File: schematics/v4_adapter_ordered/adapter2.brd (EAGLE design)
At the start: 83.1 x 45.2 mm, 40 parts, among them X1 USB-A-HU, X10 USB-A-HU, X11 USB-A-HU, X12 USB-A-HU, X13 USB-A-HU, X14 USB-A-HU, X15 USB-A-HU, X16 USB-A-HU, X17 USB-A-HU, X18 USB-A-HU, X19 USB-A-HU, X2 USB-A-HU, X20 USB-A-HU, X21 USB-A-HU, X22 USB-A-HU, X23 USB-A-HU, X24 USB-A-HU, X25 USB-A-HU, X26 USB-A-HU, X27 USB-A-HU, X28 USB-A-HU, X29 USB-A-HU, X3 USB-A-HU, X30 USB-A-HU, X31 USB-A-HU, X32 USB-A-HU, X4 USB-A-HU, X49 USB-A-HU, X5 USB-A-HU, X50 USB-A-HU, X51 USB-A-HU, X52 USB-A-HU, X53 USB-A-HU, X54 USB-A-HU, X55 USB-A-HU, X56 USB-A-HU, X6 USB-A-HU, X7 USB-A-HU, X8 USB-A-HU, X9 USB-A-HU

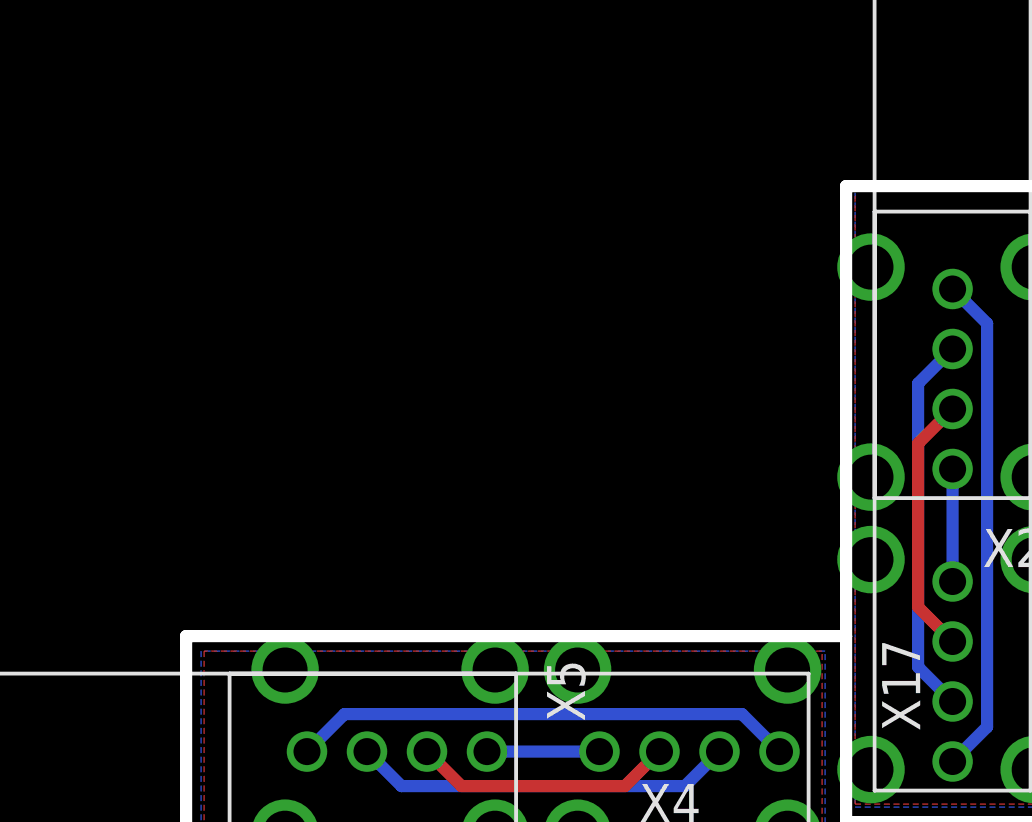
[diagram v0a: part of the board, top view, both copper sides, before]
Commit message: sch + adapter
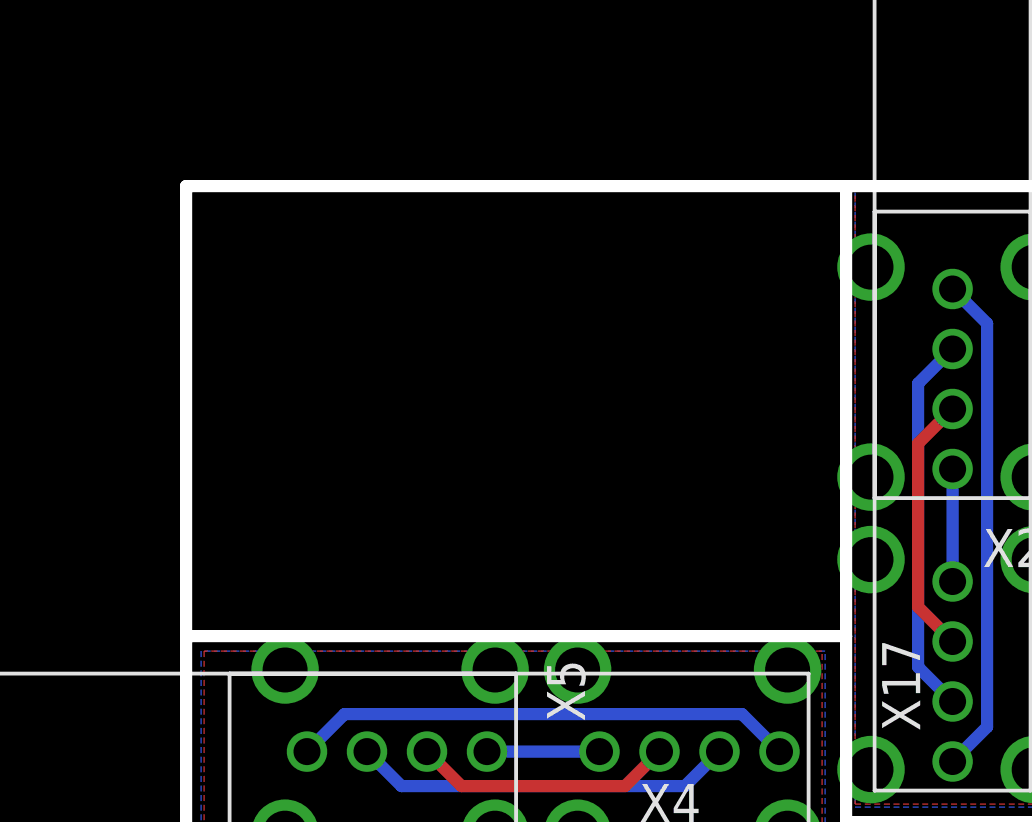
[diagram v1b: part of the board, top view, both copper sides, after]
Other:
- outline, holes or cut-outs redrawn
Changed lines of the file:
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@@
 <wire x1="31.6" y1="21.4" x2="92.7" y2="21.4" width="0.4064" layer="20"/>
 <wire x1="92.7" y1="24" x2="31.6" y2="24" width="0.4064" layer="20"/>
+<wire x1="31.6" y1="45.2" x2="9.6" y2="45.2" width="0.4064" layer="20"/>
+<wire x1="9.6" y1="30.2" x2="9.6" y2="45.2" width="0.4064" layer="20"/>
 </plain>
 <attributes>
